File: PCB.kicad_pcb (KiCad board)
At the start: 4 copper layers, 43 parts, among them J1 USB_C_Receptacle_USB2.0, J2 JST - 1.00mm 4 Pin, SW1 MX_SW_solder, SW2 MX_SW_solder, SW3 MX_SW_solder, SW4 MX_SW_solder, SW72 SW_Push, SW73 SW_Push, U1 RP2040, U3 USBLC6-2SC6, U4 3.3V Fixed Regulator, U5 ZD25D40CNJGR, Y1 12MHz Crystal 3225

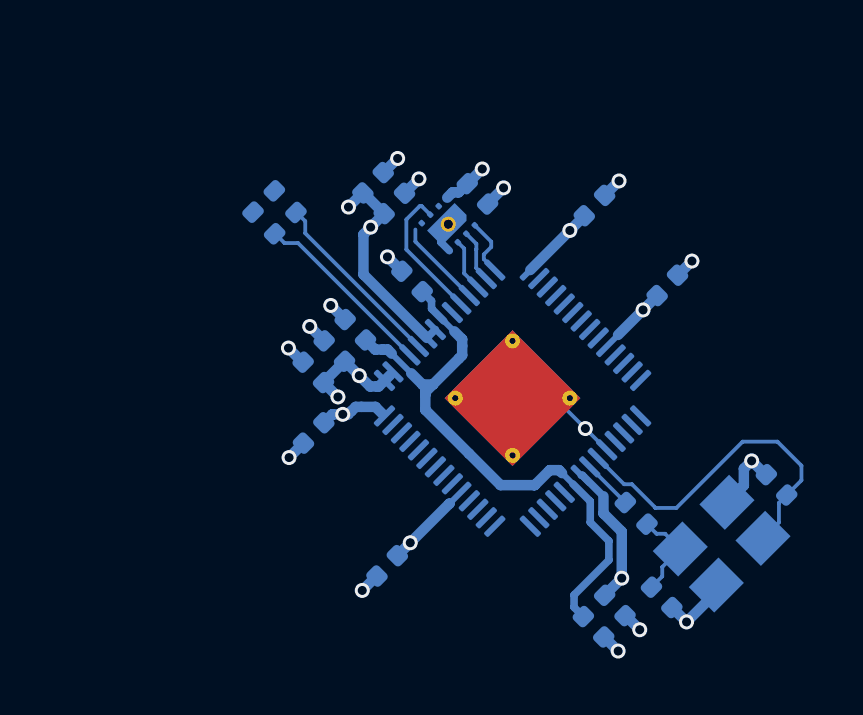
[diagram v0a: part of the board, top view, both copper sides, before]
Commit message: update to kicad 8
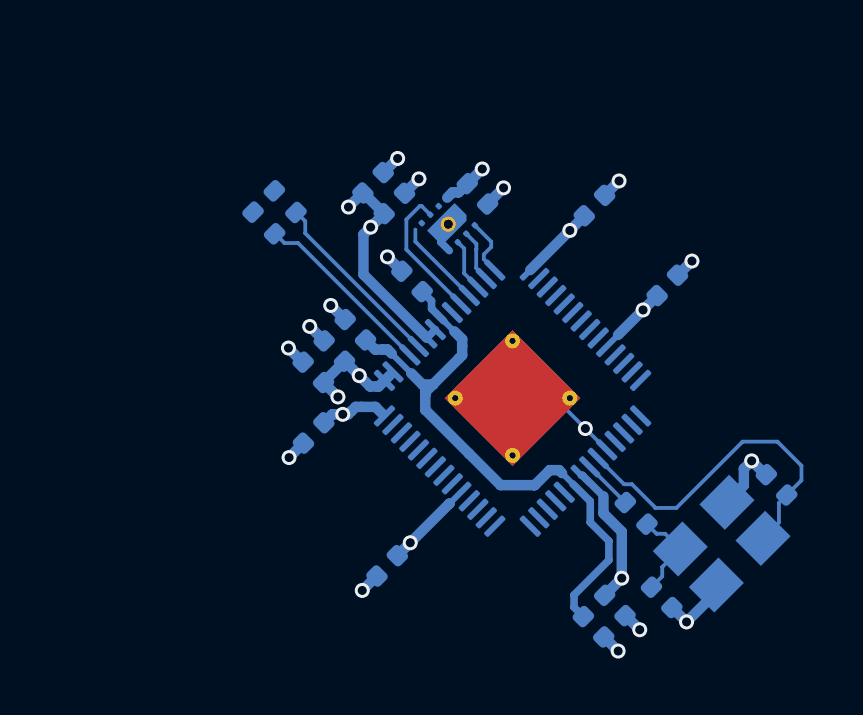
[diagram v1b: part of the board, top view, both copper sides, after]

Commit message: push de modification
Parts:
- removed D65: LED, marbastlib-mx:LED_MX_3mm
- removed SW3, SW4: MX_SW_solder, marbastlib-mx:SW_MX_1u
- removed SW72, SW73: SW_Push, Button_Switch_SMD:SW_SPST_SKQG_WithoutStem
- added ?: , , F.Cu at (240.2, 136.0)
- added ?: , , F.Cu at (330.7, 132.2)
- added ?: , , F.Cu at (335.5, 97.9)
- added ?: , , F.Cu at (140.2, 151.3)
- added ?: , , F.Cu at (92.5, 132.2)
- added ?: , , F.Cu at (343.1, 115.8)
- added ?: , , F.Cu at (140.2, 136.0)
- added ?: , , F.Cu at (306.8, 117.0)
- added ?: , , F.Cu at (330.7, 117.0)
- added ?: , , F.Cu at (68.7, 132.2)
- added ?: , , F.Cu at (306.8, 132.2)
- added ?: , , F.Cu at (335.5, 113.2)
- added ?: , , F.Cu at (61.0, 115.7)
- added ?: , , F.Cu at (311.6, 97.9)
- added ?: , , F.Cu at (250.1, 144.5)
- added ?: , , F.Cu at (311.6, 113.2)
- added ?: , , F.Cu at (337.8, 61.1)
- added ?: , , F.Cu at (314.0, 76.3)
- added ?: , , F.Cu at (337.8, 76.3)
- added ?: , , F.Cu at (314.0, 61.1)
- added ?: , , F.Cu at (68.7, 117.0)
- added ?: , , F.Cu at (240.2, 151.3)
- added ?: , , F.Cu at (92.5, 117.0)
- added A1: LP Gateron, key_switch:SW_Gateron_LowProfile_THT, F.Cu at (102.1, 106.2)
- added B1: LP Gateron, key_switch:SW_Gateron_LowProfile_THT, F.Cu at (187.8, 125.2)
- added C18: LP Gateron, key_switch:SW_Gateron_LowProfile_THT, F.Cu at (149.7, 125.2)
- added D10: D_Small, Diode_SMD:D_SOD-123, B.Cu at (107.5, 110.3)
- added D11: D_Small, Diode_SMD:D_SOD-123, B.Cu at (117.0, 129.3)
- added D12: D_Small, Diode_SMD:D_SOD-123, B.Cu at (100.3, 148.4)
- added D13: D_Small, Diode_SMD:D_SOD-123, B.Cu at (112.2, 72.2)
- added D14: D_Small, Diode_SMD:D_SOD-123, B.Cu at (121.7, 91.2)
- added D15: D_Small, Diode_SMD:D_SOD-123, B.Cu at (126.5, 110.2)
- added D16: D_Small, Diode_SMD:D_SOD-123, B.Cu at (136.1, 129.3)
- added D17: D_Small, Diode_SMD:D_SOD-123, B.Cu at (124.1, 148.4)
- added D18: LP Gateron, key_switch:SW_Gateron_LowProfile_THT, F.Cu at (140.2, 106.1)
- added D19: D_Small, Diode_SMD:D_SOD-123, B.Cu at (131.2, 72.2)
- added D20: D_Small, Diode_SMD:D_SOD-123, B.Cu at (140.8, 91.2)
- added D21: D_Small, Diode_SMD:D_SOD-123, B.Cu at (145.5, 110.2)
- added D22: D_Small, Diode_SMD:D_SOD-123, B.Cu at (155.1, 129.3)
- added D23: D_Small, Diode_SMD:D_SOD-123, B.Cu at (150.3, 72.2)
- added D24: D_Small, Diode_SMD:D_SOD-123, B.Cu at (159.8, 91.2)
- added D25: D_Small, Diode_SMD:D_SOD-123, B.Cu at (164.6, 110.2)
- added D26: D_Small, Diode_SMD:D_SOD-123, B.Cu at (174.1, 129.3)
- added D27: D_Small, Diode_SMD:D_SOD-123, B.Cu at (169.3, 72.2)
- added D28: D_Small, Diode_SMD:D_SOD-123, B.Cu at (178.8, 91.2)
- added D29: D_Small, Diode_SMD:D_SOD-123, B.Cu at (183.6, 110.2)
- added D30: D_Small, Diode_SMD:D_SOD-123, B.Cu at (193.2, 129.3)
- added D31: D_Small, Diode_SMD:D_SOD-123, B.Cu at (195.6, 148.4)
- added D32: D_Small, Diode_SMD:D_SOD-123, B.Cu at (188.4, 72.2)
- added D33: D_Small, Diode_SMD:D_SOD-123, B.Cu at (197.9, 91.2)
- added D34: D_Small, Diode_SMD:D_SOD-123, B.Cu at (202.7, 110.2)
- added D35: D_Small, Diode_SMD:D_SOD-123, B.Cu at (212.2, 129.3)
- added D36: D_Small, Diode_SMD:D_SOD-123, B.Cu at (207.4, 72.2)
- added D37: D_Small, Diode_SMD:D_SOD-123, B.Cu at (217.0, 91.2)
- added D38: D_Small, Diode_SMD:D_SOD-123, B.Cu at (221.7, 110.2)
- added D39: D_Small, Diode_SMD:D_SOD-123, B.Cu at (231.3, 129.3)
- added D40: D_Small, Diode_SMD:D_SOD-123, B.Cu at (226.5, 72.2)
- added D41: D_Small, Diode_SMD:D_SOD-123, B.Cu at (236.0, 91.2)
- added D42: D_Small, Diode_SMD:D_SOD-123, B.Cu at (240.8, 110.2)
- added D43: D_Small, Diode_SMD:D_SOD-123, B.Cu at (250.3, 129.3)
- added D44: D_Small, Diode_SMD:D_SOD-123, B.Cu at (245.6, 72.2)
- added D45: D_Small, Diode_SMD:D_SOD-123, B.Cu at (255.1, 91.2)
- added D46: D_Small, Diode_SMD:D_SOD-123, B.Cu at (259.8, 110.3)
- added D47: D_Small, Diode_SMD:D_SOD-123, B.Cu at (269.4, 129.3)
- added D48: D_Small, Diode_SMD:D_SOD-123, B.Cu at (267.0, 148.4)
- added D49: D_Small, Diode_SMD:D_SOD-123, B.Cu at (264.6, 72.2)
- added D5: D_Small, Diode_SMD:D_SOD-123, B.Cu at (81.2, 110.2)
- added D50: D_Small, Diode_SMD:D_SOD-123, B.Cu at (274.1, 91.2)
- added D51: D_Small, Diode_SMD:D_SOD-123, B.Cu at (278.9, 110.2)
- added D52: D_Small, Diode_SMD:D_SOD-123, B.Cu at (288.4, 129.4)
- added D53: D_Small, Diode_SMD:D_SOD-123, B.Cu at (290.8, 148.4)
- added D54: D_Small, Diode_SMD:D_SOD-123, B.Cu at (283.6, 72.2)
- added D55: D_Small, Diode_SMD:D_SOD-123, B.Cu at (293.1, 91.2)
- added D56: D_Small, Diode_SMD:D_SOD-123, B.Cu at (297.9, 110.2)
- added D57: D_Small, Diode_SMD:D_SOD-123, B.Cu at (314.6, 148.4)
- added D58: D_Small, Diode_SMD:D_SOD-123, B.Cu at (302.8, 72.2)
- added D59: D_Small, Diode_SMD:D_SOD-123, B.Cu at (312.2, 91.2)
- added D6: D_Small, Diode_SMD:D_SOD-123, B.Cu at (86.0, 129.3)
- added D60: D_Small, Diode_SMD:D_SOD-123, B.Cu at (331.4, 72.2)
- added D61: D_Small, Diode_SMD:D_SOD-123, B.Cu at (336.1, 91.2)
- added D62: D_Small, Diode_SMD:D_SOD-123, B.Cu at (328.9, 110.2)
- added D63: D_Small, Diode_SMD:D_SOD-123, B.Cu at (324.1, 129.3)
- added D64: D_Small, Diode_SMD:D_SOD-123, B.Cu at (338.4, 148.4)
- added D7: D_Small, Diode_SMD:D_SOD-123, B.Cu at (76.5, 148.4)
- added D8: D_Small, Diode_SMD:D_SOD-123, B.Cu at (93.2, 72.2)
- added D9: D_Small, Diode_SMD:D_SOD-123, B.Cu at (102.7, 91.2)
- added E1: LP Gateron, key_switch:SW_Gateron_LowProfile_THT, F.Cu at (135.4, 87.1)
- added F2: 700mA, Fuse:Fuse_0805_2012Metric, B.Cu at (41.7, 75.3)
- added G1: LP Gateron, key_switch:SW_Gateron_LowProfile_THT, F.Cu at (178.2, 106.1)
- added H1: LP Gateron, key_switch:SW_Gateron_LowProfile_THT, F.Cu at (197.3, 106.1)
- added H3: MountingHole, lib.pretty:PKRHSL, F.Cu at (61.0, 115.7)
- added H4: MountingHole, lib.pretty:PKRH, F.Cu at (248.1, 144.5)
- added H5: MountingHole, lib.pretty:PKRHSL, F.Cu at (343.1, 115.8)
- added I1: LP Gateron, key_switch:SW_Gateron_LowProfile_THT, F.Cu at (230.7, 87.1)
- added J3: JST - 1.00mm 4 Pin, Connector_JST:JST_SH_SM04B-SRSS-TB_1x04-1MP_P1.00mm_Horizontal, B.Cu at (63.8, 80.3)
- added K1: LP Gateron, key_switch:SW_Gateron_LowProfile_THT, F.Cu at (235.4, 106.1)
- added KB"1: LP Gateron, key_switch:SW_Gateron_LowProfile_THT, F.Cu at (292.6, 106.1)
- added KB+1: LP Gateron, key_switch:SW_Gateron_LowProfile_THT, F.Cu at (297.4, 68.0)
- added KB-1: LP Gateron, key_switch:SW_Gateron_LowProfile_THT, F.Cu at (278.3, 68.0)
- added KB1: LP Gateron, key_switch:SW_Gateron_LowProfile_THT, F.Cu at (87.8, 68.0)
- added KB10: LP Gateron, key_switch:SW_Gateron_LowProfile_THT, F.Cu at (259.3, 68.0)
- added KB2: LP Gateron, key_switch:SW_Gateron_LowProfile_THT, F.Cu at (106.8, 68.0)
- added KB3: LP Gateron, key_switch:SW_Gateron_LowProfile_THT, F.Cu at (125.9, 68.0)
- added KB4: LP Gateron, key_switch:SW_Gateron_LowProfile_THT, F.Cu at (145.0, 68.0)
- added KB5: LP Gateron, key_switch:SW_Gateron_LowProfile_THT, F.Cu at (164.0, 68.0)
- added KB6: LP Gateron, key_switch:SW_Gateron_LowProfile_THT, F.Cu at (183.1, 68.0)
- added KB7: LP Gateron, key_switch:SW_Gateron_LowProfile_THT, F.Cu at (202.1, 68.0)
- added KB8: LP Gateron, key_switch:SW_Gateron_LowProfile_THT, F.Cu at (221.2, 68.0)
- added KB9: LP Gateron, key_switch:SW_Gateron_LowProfile_THT, F.Cu at (240.2, 68.0)
- added KB:1: LP Gateron, key_switch:SW_Gateron_LowProfile_THT, F.Cu at (273.6, 106.2)
- added KB<1: LP Gateron, key_switch:SW_Gateron_LowProfile_THT, F.Cu at (245.0, 125.2)
- added KB>1: LP Gateron, key_switch:SW_Gateron_LowProfile_THT, F.Cu at (264.1, 125.2)
- added KB>2: LP Gateron, key_switch:SW_Gateron_LowProfile_THT, F.Cu at (283.1, 125.2)
- added KB\1: LP Gateron, key_switch:SW_Gateron_LowProfile_THT, F.Cu at (330.7, 87.1)
- added KB_BS1: LP Gateron, key_switch:SW_Gateron_LowProfile_THT, F.Cu at (325.9, 68.0)
- added KB_CL1: LP Gateron, key_switch:SW_Gateron_LowProfile_THT, F.Cu at (75.9, 106.1)
- added KB_COM1: LP Gateron, key_switch:SW_Gateron_LowProfile_THT, F.Cu at (95.0, 144.2)
- added KB_ESC1: LP Gateron, key_switch:SW_Gateron_LowProfile_THT, F.Cu at (68.7, 68.0)
- added KB_FN1: LP Gateron, key_switch:SW_Gateron_LowProfile_THT, F.Cu at (285.4, 144.2)
- added KB_L_ALT1: LP Gateron, key_switch:SW_Gateron_LowProfile_THT, F.Cu at (118.8, 144.2)
- added KB_L_CTLR1: LP Gateron, key_switch:SW_Gateron_LowProfile_THT, F.Cu at (71.2, 144.2)
- added KB_L_SHIFT1: LP Gateron, key_switch:SW_Gateron_LowProfile_THT, F.Cu at (80.7, 125.2)
- added KB_MENU1: LP Gateron, key_switch:SW_Gateron_LowProfile_THT, F.Cu at (309.2, 144.3)
- added KB_R_ALT1: LP Gateron, key_switch:SW_Gateron_LowProfile_THT, F.Cu at (261.6, 144.2)
- added KB_R_CTRL1: LP Gateron, key_switch:SW_Gateron_LowProfile_THT, F.Cu at (333.1, 144.2)
- added KB_R_SHIFT1: LB Gateron, key_switch:SW_Gateron_LowProfile_THT, F.Cu at (318.8, 125.2)
- added KB_SPACE1: LP Gateron, key_switch:SW_Gateron_LowProfile_THT, F.Cu at (190.2, 144.2)
- added KB_TAB1: LP Gateron, key_switch:SW_Gateron_LowProfile_THT, F.Cu at (73.5, 87.1)
- added KB_enter1: LP Gateron, key_switch:SW_Gateron_LowProfile_THT, F.Cu at (323.6, 106.1)
- added KB{1: LP Gateron, key_switch:SW_Gateron_LowProfile_THT, F.Cu at (287.8, 87.1)
- added KB}1: LP Gateron, key_switch:SW_Gateron_LowProfile_THT, F.Cu at (306.9, 87.1)
- added L1: LP Gateron, key_switch:SW_Gateron_LowProfile_THT, F.Cu at (254.4, 106.2)
- added M1: LP Gateron, key_switch:SW_Gateron_LowProfile_THT, F.Cu at (225.9, 125.2)
- added N1: LP Gateron, key_switch:SW_Gateron_LowProfile_THT, F.Cu at (206.8, 125.2)
- added O1: LP Gateron, key_switch:SW_Gateron_LowProfile_THT, F.Cu at (249.7, 87.1)
- added P1: LP Gateron, key_switch:SW_Gateron_LowProfile_THT, F.Cu at (268.8, 87.1)
- added Q1: LP Gateron, key_switch:SW_Gateron_LowProfile_THT, F.Cu at (97.3, 87.1)
- added R6: LP Gateron, key_switch:SW_Gateron_LowProfile_THT, F.Cu at (154.5, 87.1)
- added R8: 5.1k, Resistor_SMD:R_0603_1608Metric, B.Cu at (41.9, 72.5)
- added S1: LP Gateron, key_switch:SW_Gateron_LowProfile_THT, F.Cu at (121.2, 106.1)
- added T1: LP Gateron, key_switch:SW_Gateron_LowProfile_THT, F.Cu at (173.5, 87.1)
- added U2: AP7361C-33E, Package_TO_SOT_SMD:SOT-223-3_TabPin2, B.Cu at (33.6, 83.9)
- added V1: LP Gateron, key_switch:SW_Gateron_LowProfile_THT, F.Cu at (168.8, 125.2)
- added W1: LP Gateron, key_switch:SW_Gateron_LowProfile_THT, F.Cu at (116.3, 87.1)
- added X1: LP Gateron, key_switch:SW_Gateron_LowProfile_THT, F.Cu at (130.7, 125.2)
- added Y2: LP Gateron, key_switch:SW_Gateron_LowProfile_THT, F.Cu at (192.6, 87.1)
- added Z1: LP Gateron, key_switch:SW_Gateron_LowProfile_THT, F.Cu at (111.6, 125.2)
- C1, C2: value 30p -> 6pF
- C10: value 1u -> 4.7µF; footprint Capacitor_SMD:C_0402_1005Metric -> Capacitor_SMD:C_0805_2012Metric
- C11, C14, C16, C6, C8, C9: value 100n -> 100nF
- C12, C13, C15: value 1u -> 100nF
- C17, C4, C7: value 100n -> 2µ2F; footprint Capacitor_SMD:C_0402_1005Metric -> Capacitor_SMD:C_0805_2012Metric
- C3: value 1u -> 2µ2F; footprint Capacitor_SMD:C_0402_1005Metric -> Capacitor_SMD:C_0805_2012Metric
- C5: value 100n -> 4.7µF; footprint Capacitor_SMD:C_0402_1005Metric -> Capacitor_SMD:C_0805_2012Metric
- D1: value D_Small -> RED; footprint Diode_SMD:D_SOD-123 -> Diode_SMD:D_0805_2012Metric
- D2: value D_Small -> GREEN; footprint Diode_SMD:D_SOD-123 -> Diode_SMD:D_0805_2012Metric
- F1: value 700mA -> LP Gateron; footprint Fuse:Fuse_0402_1005Metric -> key_switch:SW_Gateron_LowProfile_THT; moved to F.Cu
- FB1: value 100 Ohm @ 100 MHz -> 600 Ohm @ 100 MHz; footprint Inductor_SMD:L_0402_1005Metric -> Inductor_SMD:L_0805_2012Metric
- J1: value USB_C_Receptacle_USB2.0 -> LP Gateron; footprint Connector_USB:USB_C_Receptacle_GCT_USB4085 -> key_switch:SW_Gateron_LowProfile_THT; moved to F.Cu
- J2: value JST - 1.00mm 4 Pin -> USB_C_2-0; footprint Connector_JST:JST_SH_SM04B-SRSS-TB_1x04-1MP_P1.00mm_Horizontal -> Connector_USB:USB_C_Receptacle_G-Switch_GT-USB-7010ASV
- R1, R2: value 22 -> 27; footprint Resistor_SMD:R_0402_1005Metric -> Resistor_SMD:R_0603_1608Metric
- R3: footprint Resistor_SMD:R_0402_1005Metric -> Resistor_SMD:R_0603_1608Metric
- R4, R5: value 5.1k -> 330; footprint Resistor_SMD:R_0402_1005Metric -> Resistor_SMD:R_0603_1608Metric
- R7: value R_Small_US -> 5.1k; footprint Resistor_SMD:R_0402_1005Metric -> Resistor_SMD:R_0603_1608Metric
- SW1: value MX_SW_solder -> SW_CHIP_EN; footprint marbastlib-mx:SW_MX_1u -> Button_Switch_SMD:SW_DIP_SPSTx01_Slide_6.7x4.1mm_W6.73mm_P2.54mm_LowProfile_JPin
- SW2: value MX_SW_solder -> SW_BOOT; footprint marbastlib-mx:SW_MX_1u -> Button_Switch_SMD:SW_DIP_SPSTx01_Slide_6.7x4.1mm_W6.73mm_P2.54mm_LowProfile_JPin
- U3: value USBLC6-2SC6 -> W25Q16JVSSIQ; footprint Package_TO_SOT_SMD:SOT-23-6 -> Package_SO:SOIC-8_5.23x5.23mm_P1.27mm
- U4: value 3.3V Fixed Regulator -> LP Gateron; footprint Package_TO_SOT_SMD:TSOT-23 -> key_switch:SW_Gateron_LowProfile_THT; moved to F.Cu
- U5: value ZD25D40CNJGR -> USBLC6-2SC6; footprint USON8:USON-8_1.5x1.5mm_P0.45mm -> Package_TO_SOT_SMD:SOT-23-6
- Y1: value 12MHz Crystal 3225 -> STDCRG1-12M
- moved SW2 181.8 mm to (205.0, 144.2), turned to 90 degrees
- moved SW1 167.7 mm to (175.0, 144.2), turned to 90 degrees
- moved R3 130.1 mm to (26.4, 101.0), turned to 180 degrees
- moved C9 127.9 mm to (32.7, 103.6), turned to 180 degrees
- moved C1 127.6 mm to (32.7, 95.7), turned to 180 degrees
- moved C16 125.1 mm to (29.8, 103.6), turned to 180 degrees
- moved C11 123.7 mm to (32.7, 105.6), turned to 180 degrees
- moved C2 123.5 mm to (32.7, 97.7), turned to 180 degrees
- moved J1 123.4 mm to (216.3, 106.1), turned to 0 degrees
- moved C17 123.3 mm to (36.3, 104.5), turned to 180 degrees
- moved C14 121.3 mm to (29.8, 99.7), turned to 180 degrees
- moved C10 118.8 mm to (36.3, 101.5), turned to 180 degrees
- moved C12 117.9 mm to (29.8, 95.7), turned to 180 degrees
- moved C8 115.7 mm to (32.7, 101.6), turned to 180 degrees
- moved C6 115.4 mm to (32.7, 99.7), turned to 180 degrees
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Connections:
- net Net-(U1-USB_DM) renamed /DrN
- net Net-(U1-USB_DP) renamed /DrP
- C12 pad 1: +1V1 -> +3.3V
- C13 pad 1: /VFused_ -> +3.3V
- C14 pad 1: +1V1 -> +3.3V
- C16 pad 1: +1V1 -> +3.3V
- C3 pad 1: +3.3V -> +1V1
- C5 pad 1: +3.3V -> V_Fused
- C6 pad 1: +3.3V -> +1V1
- C8 pad 1: +3.3V -> +1V1
- D1 pad 1: GP0 -> Net-(D1-K)
- D1 pad 2: Net-(D1-A) -> +3.3V
- D2 pad 1: GP0 -> Net-(D2-K)
- D2 pad 2: Net-(D2-A) -> +3.3V
- D3 pad 1: GP1 -> GP14
- D4 pad 1: GP1 -> GP15
- F1 pad 1: Net-(F1-Pad1) -> GP4
- F1 pad 2: /VBUS -> Net-(D25-A)
- FB1 pad 1: Net-(F1-Pad1) -> Net-(F2-Pad1)
- FB1 pad 2: /VFused_ -> V_Fused
- R4 pad 1: GND -> Net-(D1-K)
- R4 pad 2: Net-(J1-CC1) -> GP25
- R5 pad 1: GND -> Net-(D2-K)
- R5 pad 2: Net-(J1-CC2) -> GND
- R7 pad 1: Net-(D65-K) -> GND
- R7 pad 2: /LED_INDICATOR -> Net-(J2-CC2)
- SW1 pad 1: GP2 -> GND
- SW1 pad 2: Net-(D1-A) -> /RUN_
- SW2 pad 1: GP3 -> GND
- SW2 pad 2: Net-(D2-A) -> /CS_
- U3 pad 1: /DN -> /CS_
- U3 pad 2: GND -> /SD1_
- U3 pad 3: /DP -> /SD2_
- U3 pad 4: /D1+ -> GND
- U3 pad 5: /VBUS -> /SD0_
- U3 pad 6: /D1- -> /SCLK_
- U4 pad 1: GND -> GP7
- U4 pad 2: +3.3V -> Net-(D37-A)
- U5 pad 1: /CS_ -> /USB-C/DN
- U5 pad 2: /SD1_ -> GND
- U5 pad 3: /SD2_ -> /USB-C/DP
- U5 pad 4: GND -> /USB-C/D1+
- U5 pad 5: /SD0_ -> /USB-C/VBUS
- U5 pad 6: /SCLK_ -> /USB-C/D1-
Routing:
- net +3.3V: track 26.6 -> 0.00 mm, vias 10 -> 0
- net +1V1: track 18.6 -> 0.00 mm
- net GND: track 18.6 -> 0.00 mm, vias 16 -> 0
- net /XIN_: track 11.7 -> 0.00 mm
- net /DrN: track 6.18 -> 0.00 mm
- net /DrP: track 6.17 -> 0.00 mm
- net /SCLK_: track 4.67 -> 0.00 mm
- net /XOUT_: track 3.12 -> 0.00 mm
- net /SD0_: track 2.95 -> 0.00 mm
- net /CS_: track 1.97 -> 0.00 mm
- net /SD1_: track 1.78 -> 0.00 mm
- net /SD2_: track 1.77 -> 0.00 mm
- net Net-(U1-XOUT): track 1.68 -> 0.00 mm
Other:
- board outline added: 285 x 95 mm
